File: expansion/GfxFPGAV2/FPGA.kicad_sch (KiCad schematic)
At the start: 26 parts, among them J1 JTAG, U2 XC6SLX9-FTG256, U302 W25Q64JVSSIM, Y1 ECS-3963

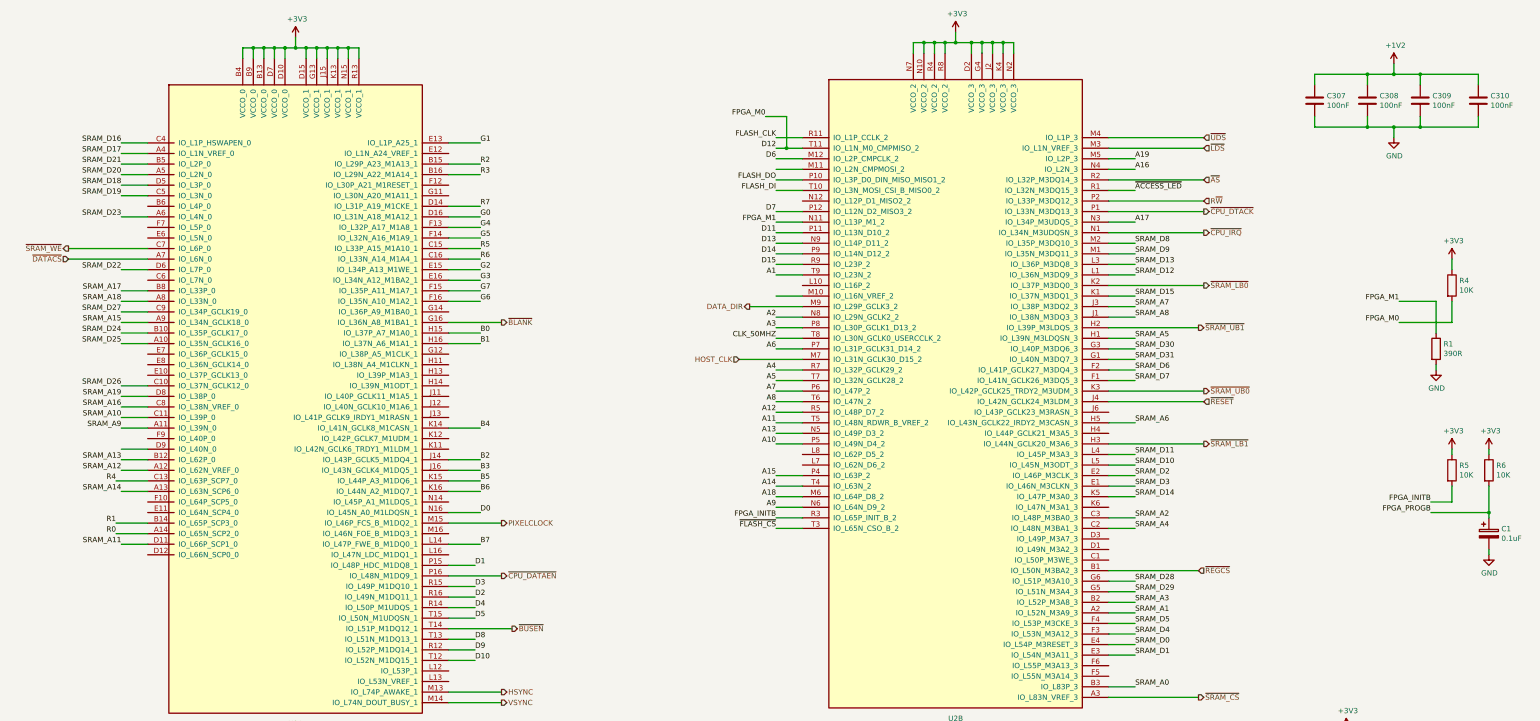
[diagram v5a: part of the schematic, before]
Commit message: VGA board v2 routing done
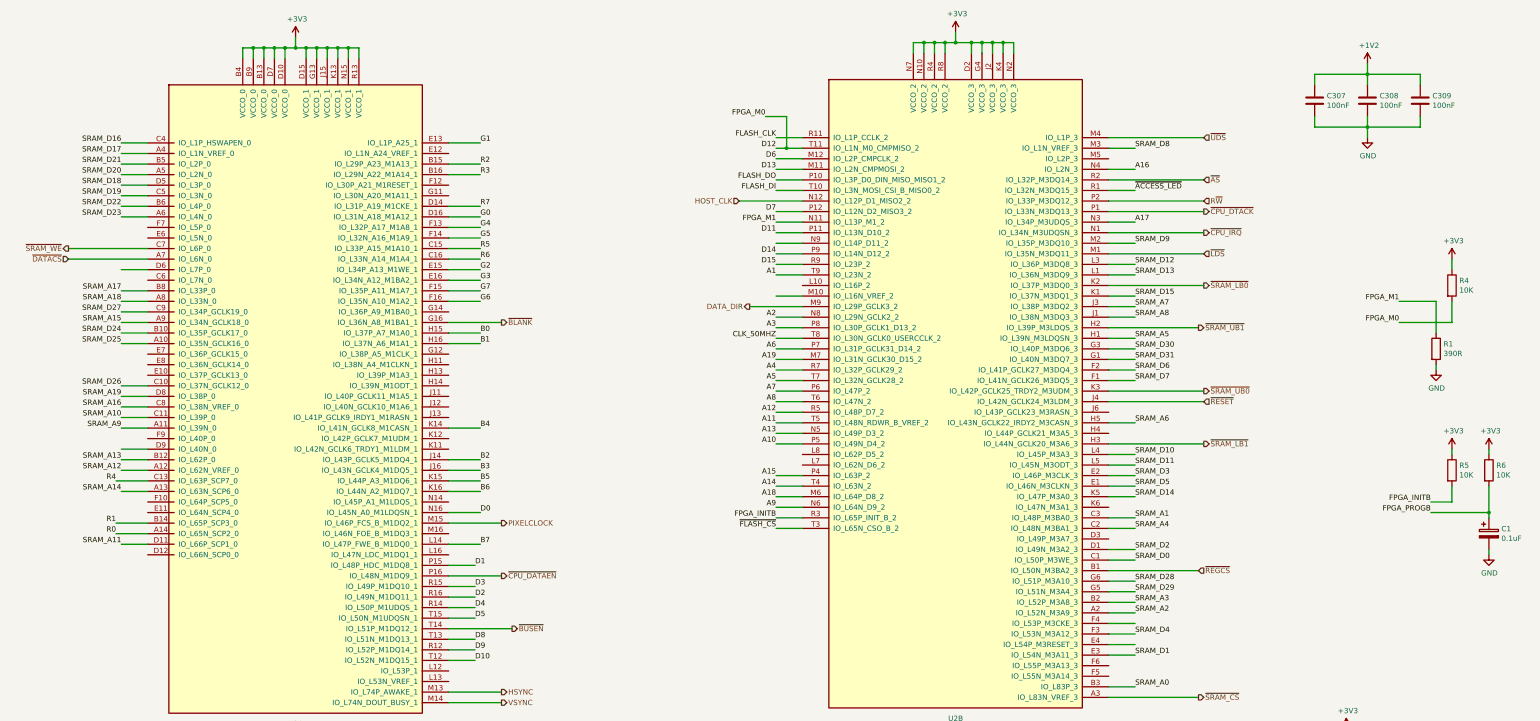
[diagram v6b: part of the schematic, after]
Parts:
- removed C310: 100nF, Capacitor_SMD:C_0805_2012Metric, symbol Device:C
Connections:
- net A19: now also U2.M7 (IO_L31N_GCLK30_D15_2); no longer U2.M5 (IO_L2P_3)
- net D13: now also U2.M11 (IO_L2N_CMPMOSI_2); no longer U2.N9 (IO_L14P_D11_2)
- net HOST_CLK: now also U2.N12 (IO_L12P_D1_MISO2_2); no longer U2.M7 (IO_L31N_GCLK30_D15_2)
- net SRAM_A1: now also U2.C3 (IO_L48P_M3BA0_3); no longer U2.A2 (IO_L52N_M3A9_3)
- net SRAM_A2: now also U2.A2 (IO_L52N_M3A9_3); no longer U2.C3 (IO_L48P_M3BA0_3)
- net SRAM_D0: now also U2.C1 (IO_L50P_M3WE_3); no longer U2.E4 (IO_L54P_M3RESET_3)
- net SRAM_D10: now also U2.L4 (IO_L45P_M3A3_3); no longer U2.L5 (IO_L45N_M3ODT_3)
- net SRAM_D11: now also U2.L5 (IO_L45N_M3ODT_3); no longer U2.L4 (IO_L45P_M3A3_3)
- net SRAM_D12: now also U2.L3 (IO_L36P_M3DQ8_3); no longer U2.L1 (IO_L36N_M3DQ9_3)
- net SRAM_D13: now also U2.L1 (IO_L36N_M3DQ9_3); no longer U2.L3 (IO_L36P_M3DQ8_3)
- net SRAM_D2: now also U2.D1 (IO_L49N_M3A2_3); no longer U2.E2 (IO_L46P_M3CLK_3)
- net SRAM_D22: now also U2.B6 (IO_L4P_0); no longer U2.D6 (IO_L7P_0)
- net SRAM_D3: now also U2.E2 (IO_L46P_M3CLK_3); no longer U2.E1 (IO_L46N_M3CLKN_3)
- net SRAM_D5: now also U2.E1 (IO_L46N_M3CLKN_3); no longer U2.F4 (IO_L53P_M3CKE_3)
- net SRAM_D8: now also U2.M3 (IO_L1N_VREF_3); no longer U2.M2 (IO_L35P_M3DQ10_3)
- net SRAM_D9: now also U2.M2 (IO_L35P_M3DQ10_3); no longer U2.M1 (IO_L35N_M3DQ11_3)
- net ~{LDS}: now also U2.M1 (IO_L35N_M3DQ11_3); no longer U2.M3 (IO_L1N_VREF_3)
